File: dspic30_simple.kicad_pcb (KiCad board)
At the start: 2 copper layers, 95.5 x 65 mm, 22 parts, among them J1 Jack-DC, J2 Conn_01x19_Pin, J4 Conn_01x21_Pin, J6 Conn_PIC_ICSP_ICD, SW1 SW_Push, U1 PIC18F4550-IP, U2 L7805, Y1 Crystal

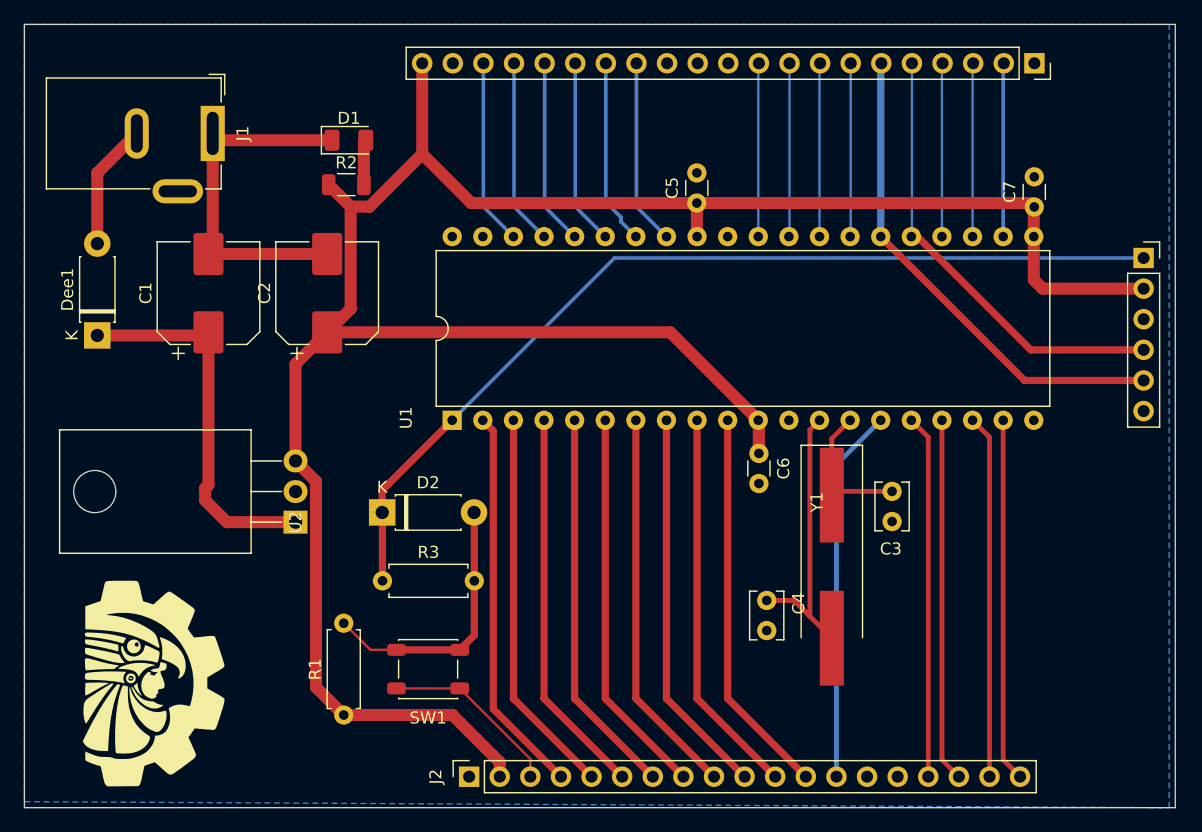
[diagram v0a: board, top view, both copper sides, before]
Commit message: changes smd component for tht components
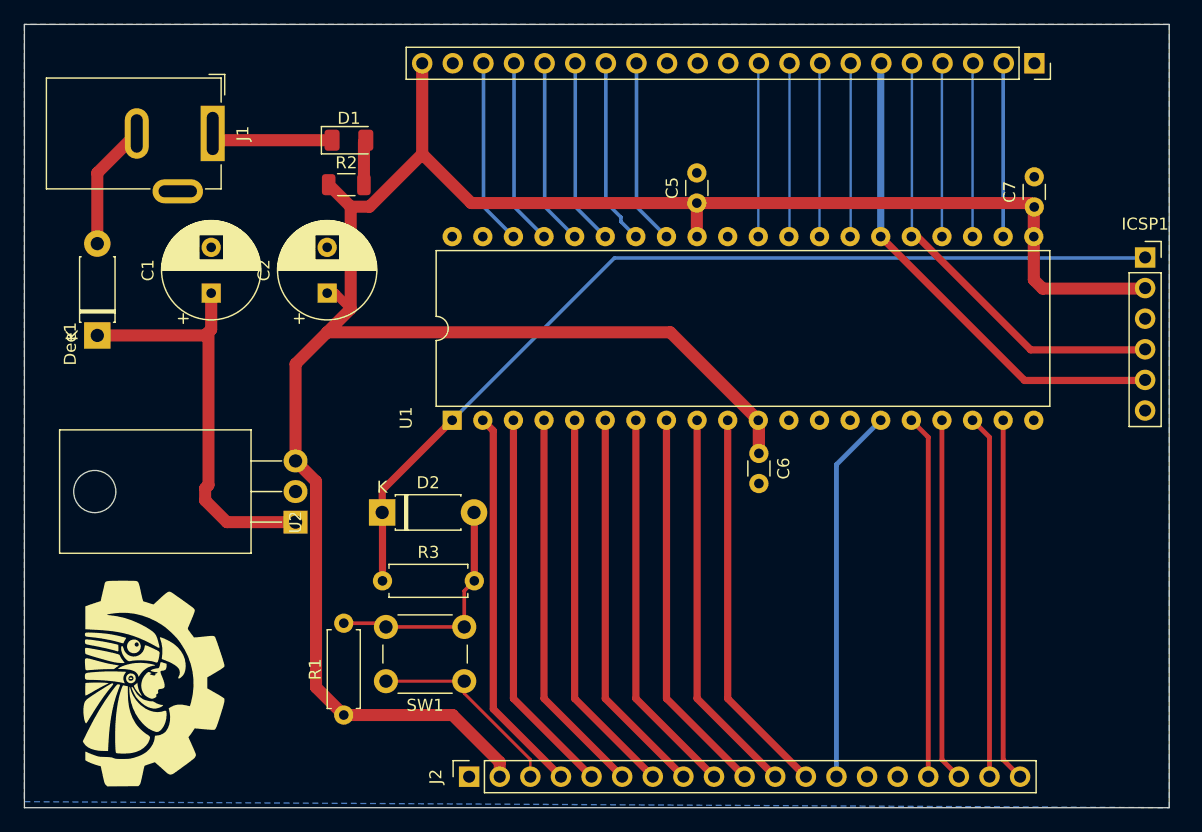
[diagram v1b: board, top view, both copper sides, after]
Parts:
- removed C3, C4: 18pF, Capacitor_THT:C_Disc_D3.8mm_W2.6mm_P2.50mm
- removed J6: Conn_PIC_ICSP_ICD, Connector_PinSocket_2.54mm:PinSocket_1x06_P2.54mm_Vertical
- removed Y1: Crystal, Crystal:Crystal_SMD_HC49-SD_HandSoldering
- added ICSP1: Conn_PIC_ICSP_ICD, Connector_PinSocket_2.54mm:PinSocket_1x06_P2.54mm_Vertical, F.Cu at (171.0, 72.3)
- C1, C2: footprint Capacitor_SMD:CP_Elec_8x10 -> Capacitor_THT:CP_Radial_D8.0mm_P3.80mm
- SW1: footprint Button_Switch_SMD:SW_SPST_PTS647_Sx38 -> Button_Switch_THT:SW_PUSH_6mm
- moved SW1 3.16 mm to (114.5, 107.5)
- moved C1 0.22 mm to (93.5, 75.3)
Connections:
- U1 pad 12: unconnected-(U1-VSS-Pad12) -> GND
- U1 pad 13: Net-(U1-OSC1/CLKI) -> unconnected-(U1-OSC1/CLKI-Pad13)
- U1 pad 14: Net-(U1-RA6/OSC2/CLKO) -> /RB6
- U1 pad 31: unconnected-(U1-VSS-Pad31) -> GND
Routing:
- net Net-(U1-OSC1/CLKI): track 23.3 -> 0.00 mm
- net GND: track 45.2 -> 27.0 mm
- net Net-(U1-RA6/OSC2/CLKO): track 12.5 -> 0.00 mm
- net Net-(Dee1-K): track 31.6 -> 35.6 mm
- net /5VLDO: track 194.4 -> 196.9 mm
- net /RESET_BOTON: track 22.5 -> 20.0 mm
- net /RB6: track 32.3 -> 32.8 mm
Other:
- board size 95.5 x 65 mm -> 95 x 65 mm

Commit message: GND DRC warnings
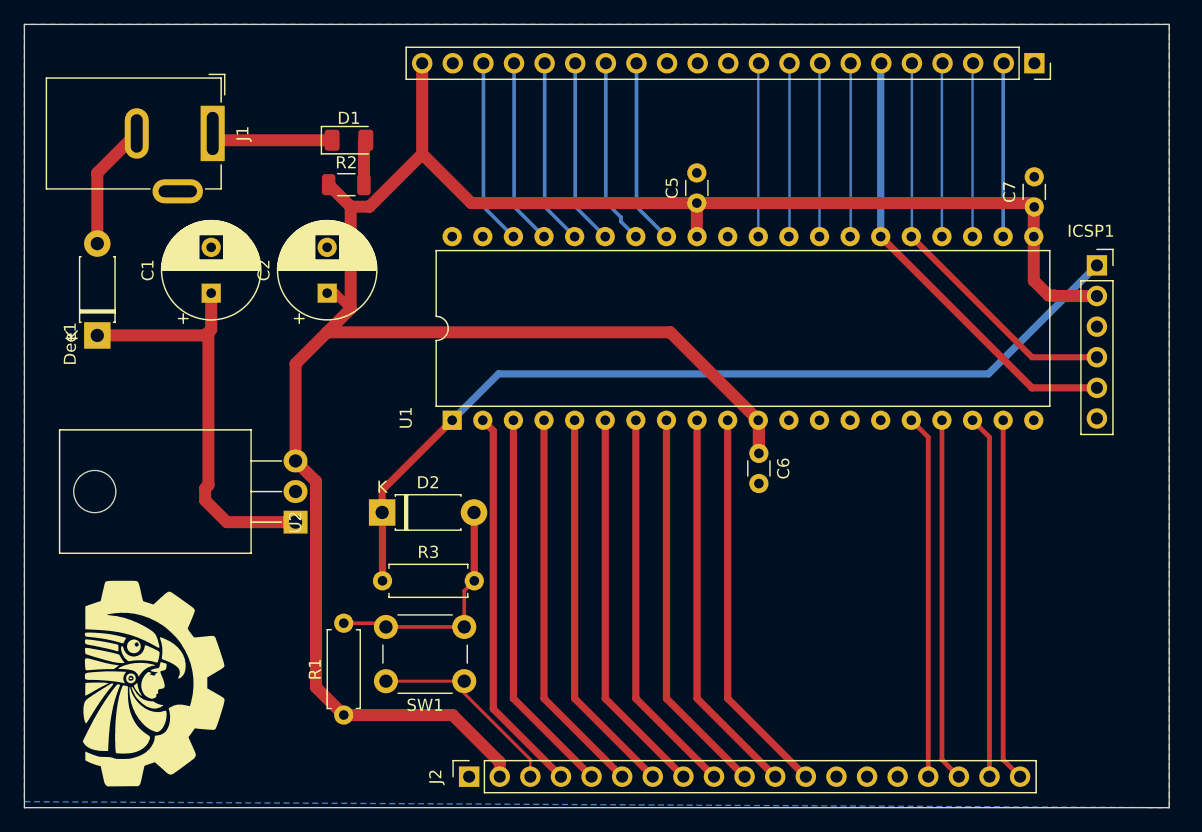
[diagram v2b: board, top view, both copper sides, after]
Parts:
- moved ICSP1 4.05 mm to (167.0, 73.0)
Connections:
- J2 pad 13: /RC13 -> /CLKI
- J2 pad 14: GND -> /RC15
- J2 pad 15: GND -> /RC13
- U1 pad 13: unconnected-(U1-OSC1/CLKI-Pad13) -> /CLKI
- U1 pad 14: /RB6 -> /RC15
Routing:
- net /RC13: track 31.1 -> 0.00 mm
- net /RESET: track 78.7 -> 74.6 mm
- net /PGC: track 41.2 -> 37.5 mm
- net /5VLDO: track 196.9 -> 193.3 mm
- net /PGD: track 37.6 -> 34.5 mm
- net /RC15: track 0.00 -> 0.54 mm
- net /RB6: track 32.8 -> 32.3 mm
